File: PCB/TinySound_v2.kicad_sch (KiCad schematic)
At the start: 9 parts

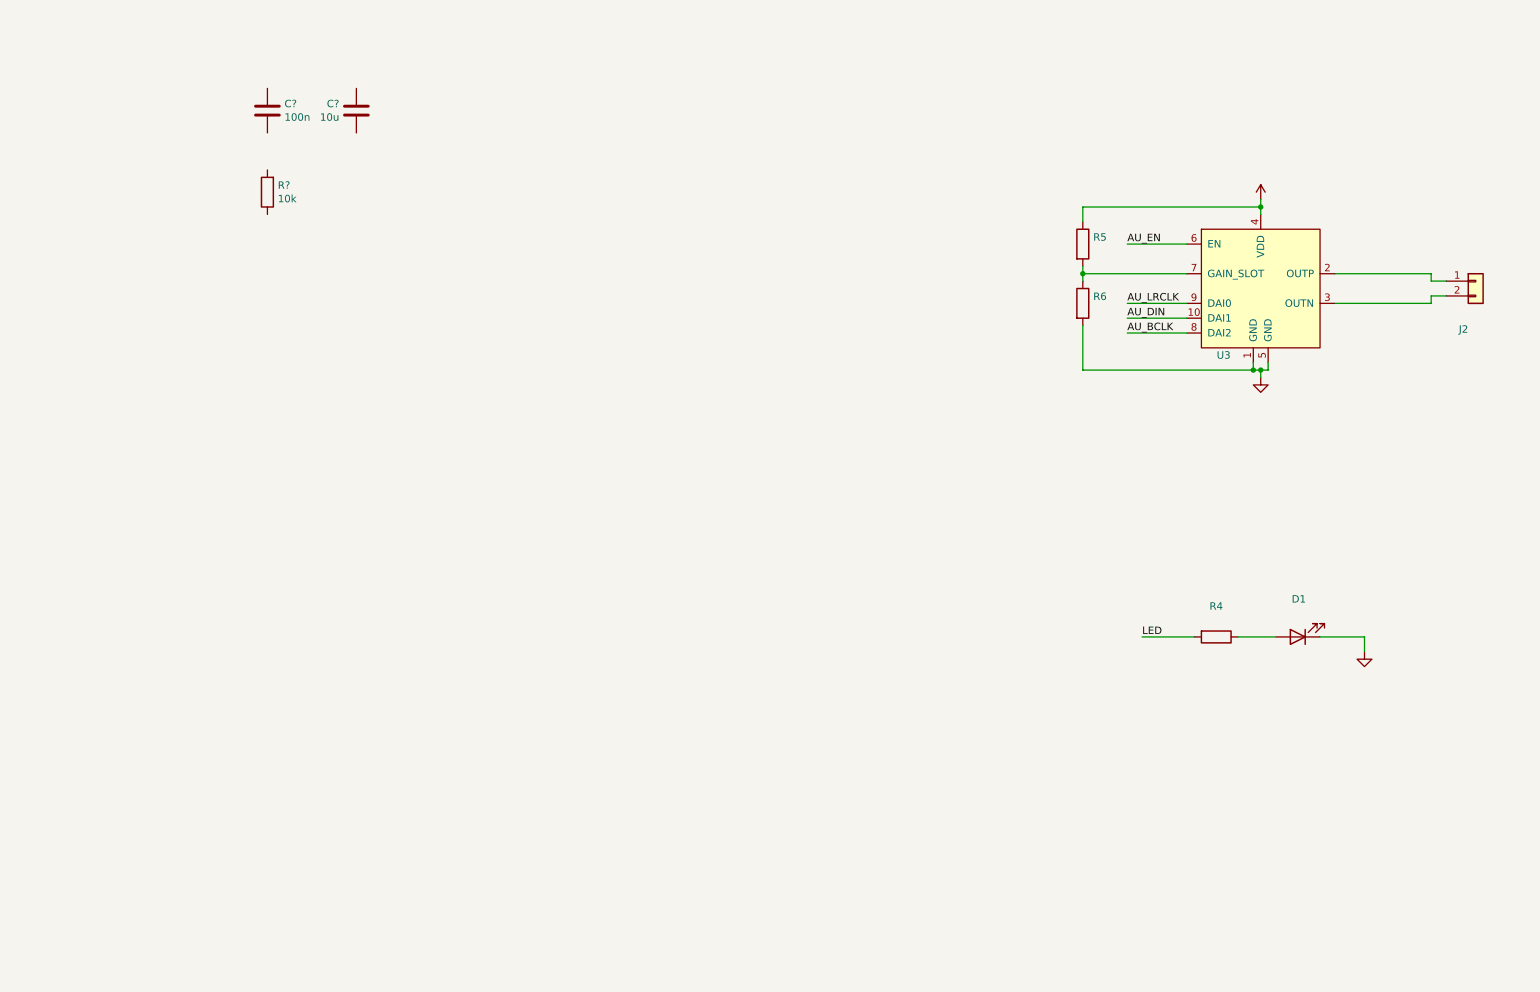
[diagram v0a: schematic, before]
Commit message: Added all components in schematic
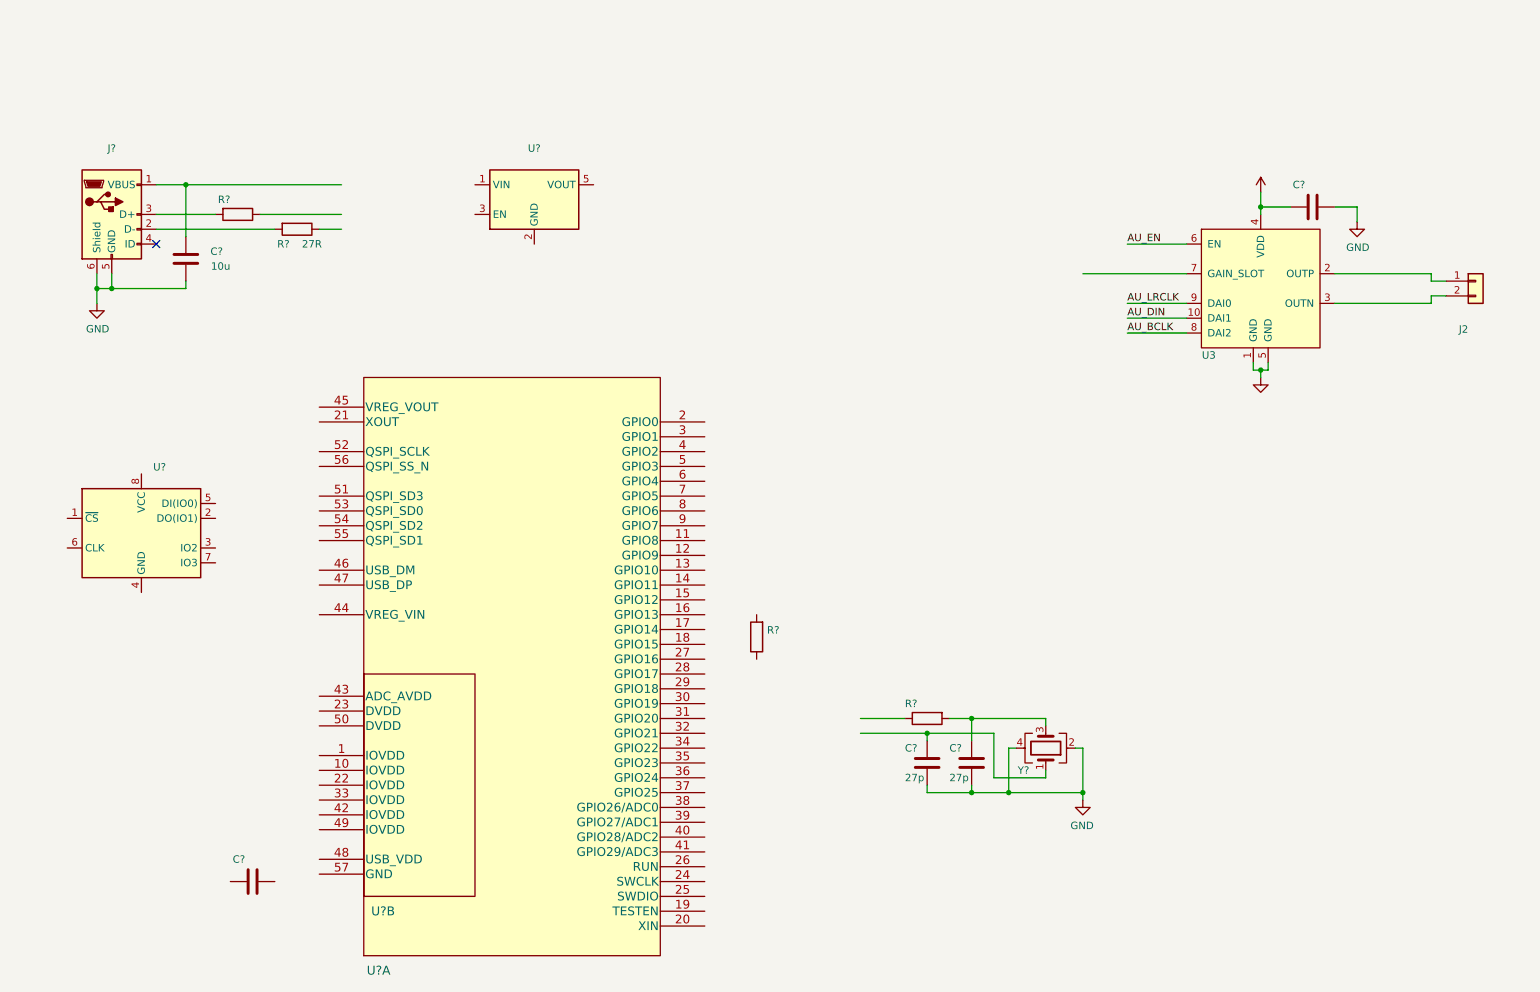
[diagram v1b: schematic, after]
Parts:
- removed D1: (no value), symbol Device:LED
- removed R4, R5, R6: (no value), symbol Device:R
- added C? (x2): 27p, Capacitor_SMD:C_0402_1005Metric, symbol Device:C
- added C?: (no value), symbol Device:C
- added J?: (no value), symbol Connector:USB_B_Micro
- added R?: (no value), symbol Device:R
- added R?: 27R, Resistor_SMD:R_0402_1005Metric, symbol Device:R
- added R?: (no value), Resistor_SMD:R_0402_1005Metric, symbol Device:R
- added U?: (no value), symbol Regulator_Linear:MIC5504-3.3YM5
- added U?: (no value), symbol Memory_Flash:W25Q128JVS
- added U? (x2): (no value), symbol TinySound:RP2040
- added Y?: (no value), symbol Device:Crystal_GND24
- C?: footprint Capacitor_SMD:C_0603_1608Metric -> (none)
- C?: value 100n -> (none); footprint Capacitor_SMD:C_0603_1608Metric -> (none)
- R?: value 10k -> (none); footprint Resistor_SMD:R_0603_1608Metric -> (none)
- U3: footprint (none) -> TinySound:FC2QFN-10
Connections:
- net +3V3: now also C?.1
- net GND: now also C?.1, C?.2, C?.1, C?.1, J?.5 (GND), J?.6 (Shield), Y?.2, Y?.4
- net at C?.2: now also J?.1 (VBUS)
- new net: J?.3 (D+), R?.2
- new net: C?.2, Y?.1
- new net: C?.2, R?.2, Y?.3
- new net: J?.2 (D-), R?.2
- no-connect marks 0 -> 1
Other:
- moved on the sheet: C?, R?

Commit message: RP2040 power, flash, crystal and reset
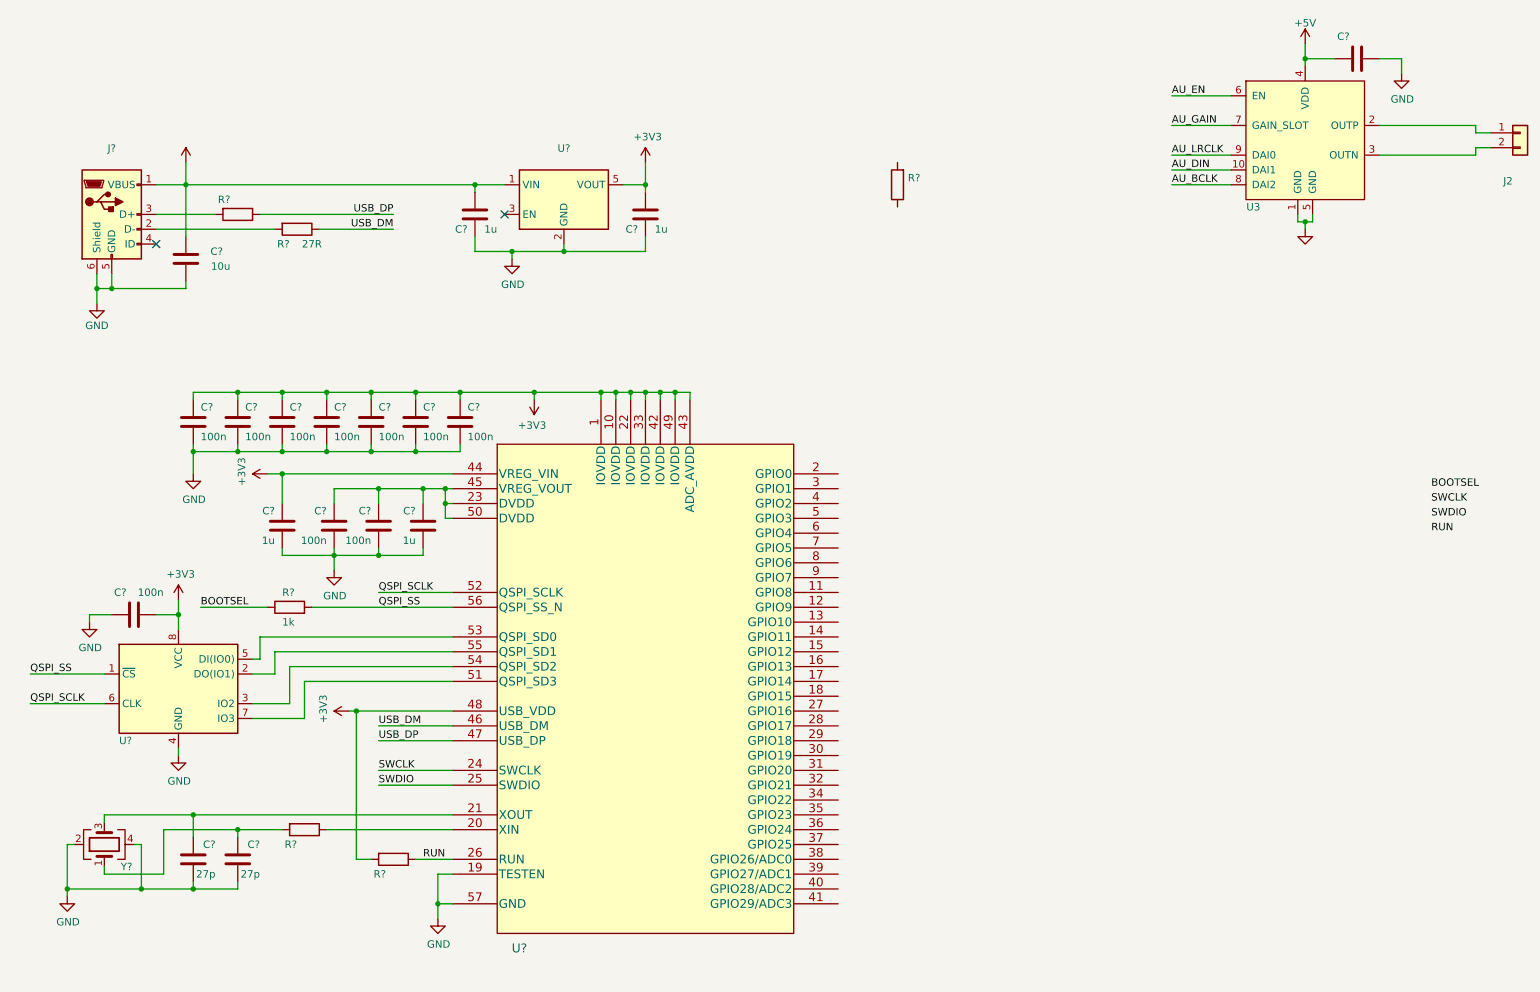
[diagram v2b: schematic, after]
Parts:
- removed C?: (no value), symbol Device:C
- removed U?: (no value), symbol TinySound:RP2040
- added C? (x10): 100n, Capacitor_SMD:C_0402_1005Metric, symbol Device:C
- added C? (x4): 1u, Capacitor_SMD:C_0402_1005Metric, symbol Device:C
- added R?: (no value), Resistor_SMD:R_0402_1005Metric, symbol Device:R
- added R?: 1k, Resistor_SMD:R_0402_1005Metric, symbol Device:R
- U?: footprint (none) -> Package_TO_SOT_SMD:SOT-23-5
- U?: footprint (none) -> Package_SO:SOIC-8_5.23x5.23mm_P1.27mm
- U?: footprint (none) -> TinySound:QFN-56_EP_7x7_Pitch0.4mm
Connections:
- net +3V3: now also U?.1 (IOVDD), U?.10 (IOVDD), U?.22 (IOVDD), U?.33 (IOVDD), U?.42 (IOVDD), U?.43 (ADC_AVDD), U?.44 (VREG_VIN), U?.48 (USB_VDD), U?.49 (IOVDD), U?.5 (VOUT), U?.8 (VCC), C?.2, C?.2, C?.2, C?.2, C?.2, C?.2, C?.2, C?.2, C?.2, C?.2, R?.2; no longer C?.1, U3.4 (VDD)
- net GND: now also U?.19 (TESTEN), U?.2 (GND), U?.4 (GND), U?.57 (GND), C?.1, C?.1, C?.1, C?.1, C?.1, C?.1, C?.1, C?.1, C?.1, C?.1, C?.1, C?.1, C?.1, C?.1
- net AU_GAIN: now reaches U3.7 (GAIN_SLOT)
- net +5V: now reaches U?.1 (VIN)
- net +5V: now also C?.1, C?.2, J?.1 (VBUS), U3.4 (VDD), C?.2
- net USB_DP: now reaches R?.1
- net USB_DP: now also U?.47 (USB_DP)
- net at C?.2, Y?.1: now also R?.2
- net at C?.2, Y?.3: now also U?.21 (XOUT); no longer R?.2
- net QSPI_SS: now reaches U?.1 (~{CS})
- net QSPI_SS: now also U?.56 (QSPI_SS_N), R?.2
- net at U?.2 (DO(IO1)): now also U?.55 (QSPI_SD1)
- net at U?.3 (IO2): now also U?.54 (QSPI_SD2)
- net at U?.5 (DI(IO0)): now also U?.53 (QSPI_SD0)
- net QSPI_SCLK: now reaches U?.6 (CLK)
- net QSPI_SCLK: now also U?.52 (QSPI_SCLK)
- net at U?.7 (IO3): now also U?.51 (QSPI_SD3)
- net USB_DM: now reaches R?.1
- net USB_DM: now also U?.46 (USB_DM)
- net at U?.20 (XIN): now also R?.1
- net SWCLK: now reaches U?.24 (SWCLK)
- net SWDIO: now reaches U?.25 (SWDIO)
- net RUN: now reaches U?.26 (RUN)
- net RUN: now also R?.1
- net at U?.45 (VREG_VOUT): now also U?.23 (DVDD), U?.50 (DVDD), C?.2, C?.2, C?.2
- new net BOOTSEL: R?.1
- no-connect marks 1 -> 2
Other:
- moved on the sheet: C?, J2, R?, U3, U?, Y?

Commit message: Finished first version of schematic
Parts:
- removed R?: (no value), symbol Device:R
- added J?: Conn_01x07, symbol Connector_Generic:Conn_01x07
- added J?: (no value), symbol Connector_Generic:Conn_01x07
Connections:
- net +3V3: now also J?.2 (Pin_2)
- net +5V: now also J?.1 (Pin_1)
- net AU_BCLK: now also U?.6 (GPIO4)
- net AU_DIN: now also U?.8 (GPIO6)
- net AU_LRCLK: now also U?.7 (GPIO5)
- net BOOTSEL: now also J?.3 (Pin_3)
- net GND: now also J?.7 (Pin_7), J?.7 (Pin_7)
- net RUN: now also J?.6 (Pin_6)
- net SWCLK: now also J?.4 (Pin_4)
- net SWDIO: now also J?.5 (Pin_5)
- net at C?.2, Y?.1: now also U?.20 (XIN); no longer R?.2
- net at C?.2, Y?.3: now also R?.2; no longer U?.21 (XOUT)
- net UART_TX: now reaches U?.2 (GPIO0)
- net UART_TX: now also J?.1 (Pin_1)
- net at R?.1: now also U?.21 (XOUT); no longer U?.20 (XIN)
- net UART_RX: now reaches U?.3 (GPIO1)
- net UART_RX: now also J?.2 (Pin_2)
- net GPIO/ADC: now reaches U?.38 (GPIO26/ADC0)
- net GPIO/ADC: now also J?.6 (Pin_6)
- new net GPIO1: J?.3 (Pin_3)
- new net GPIO2: J?.4 (Pin_4)
- new net GPIO3: J?.5 (Pin_5)
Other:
- moved on the sheet: C?, J2, R?, U3

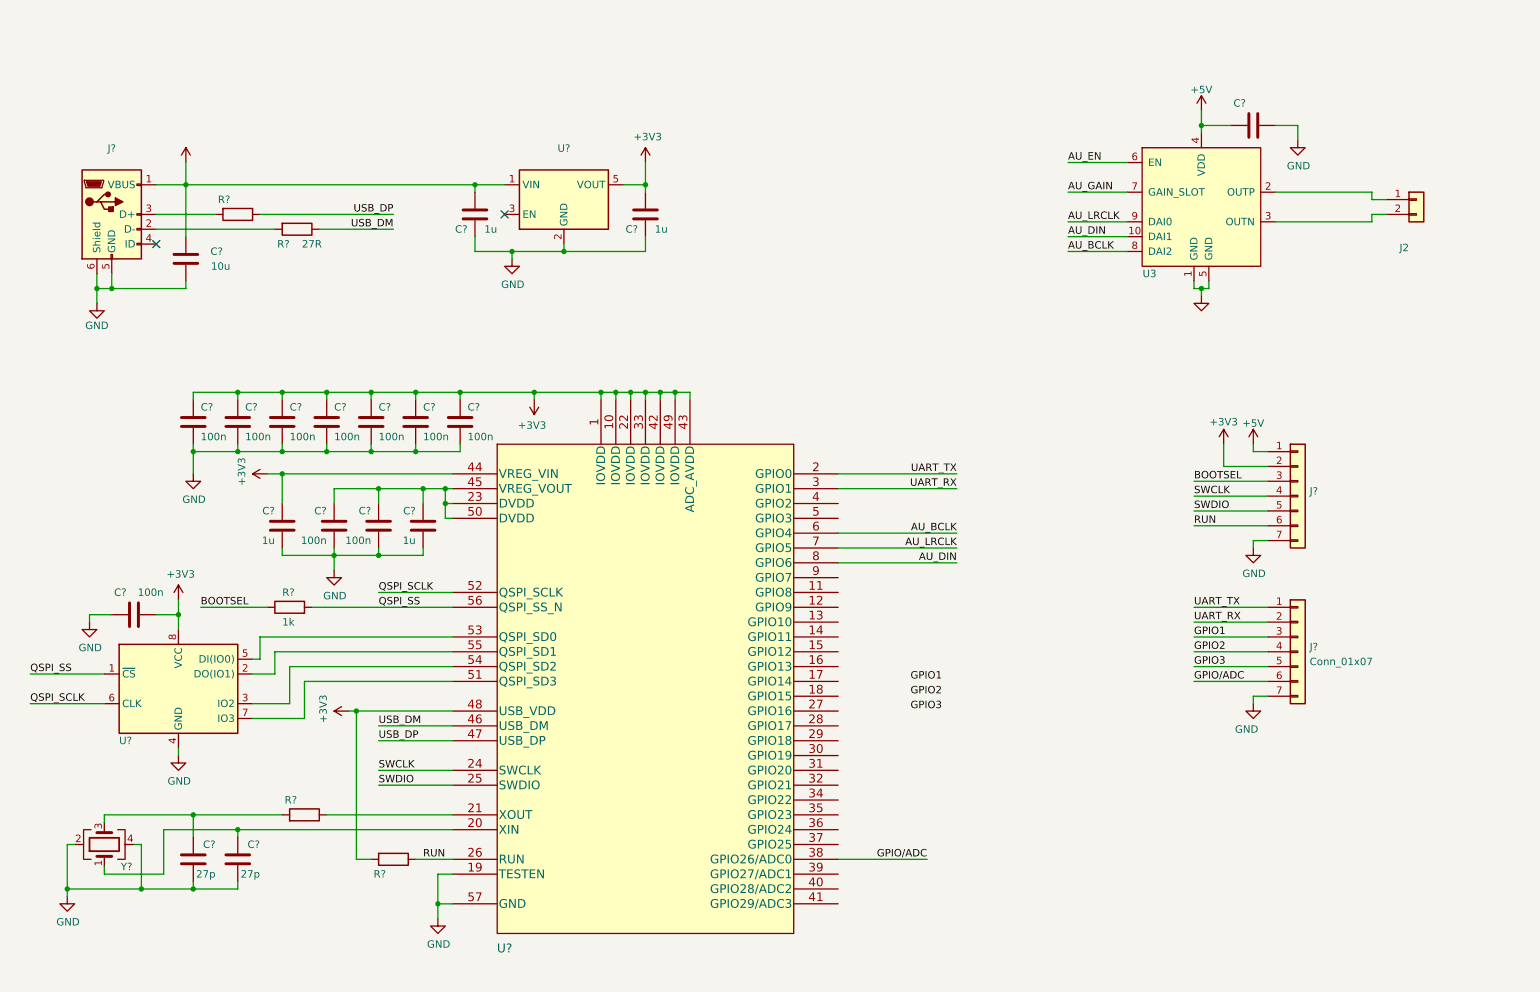
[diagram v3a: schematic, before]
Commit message: Added footprints, annoted schematic
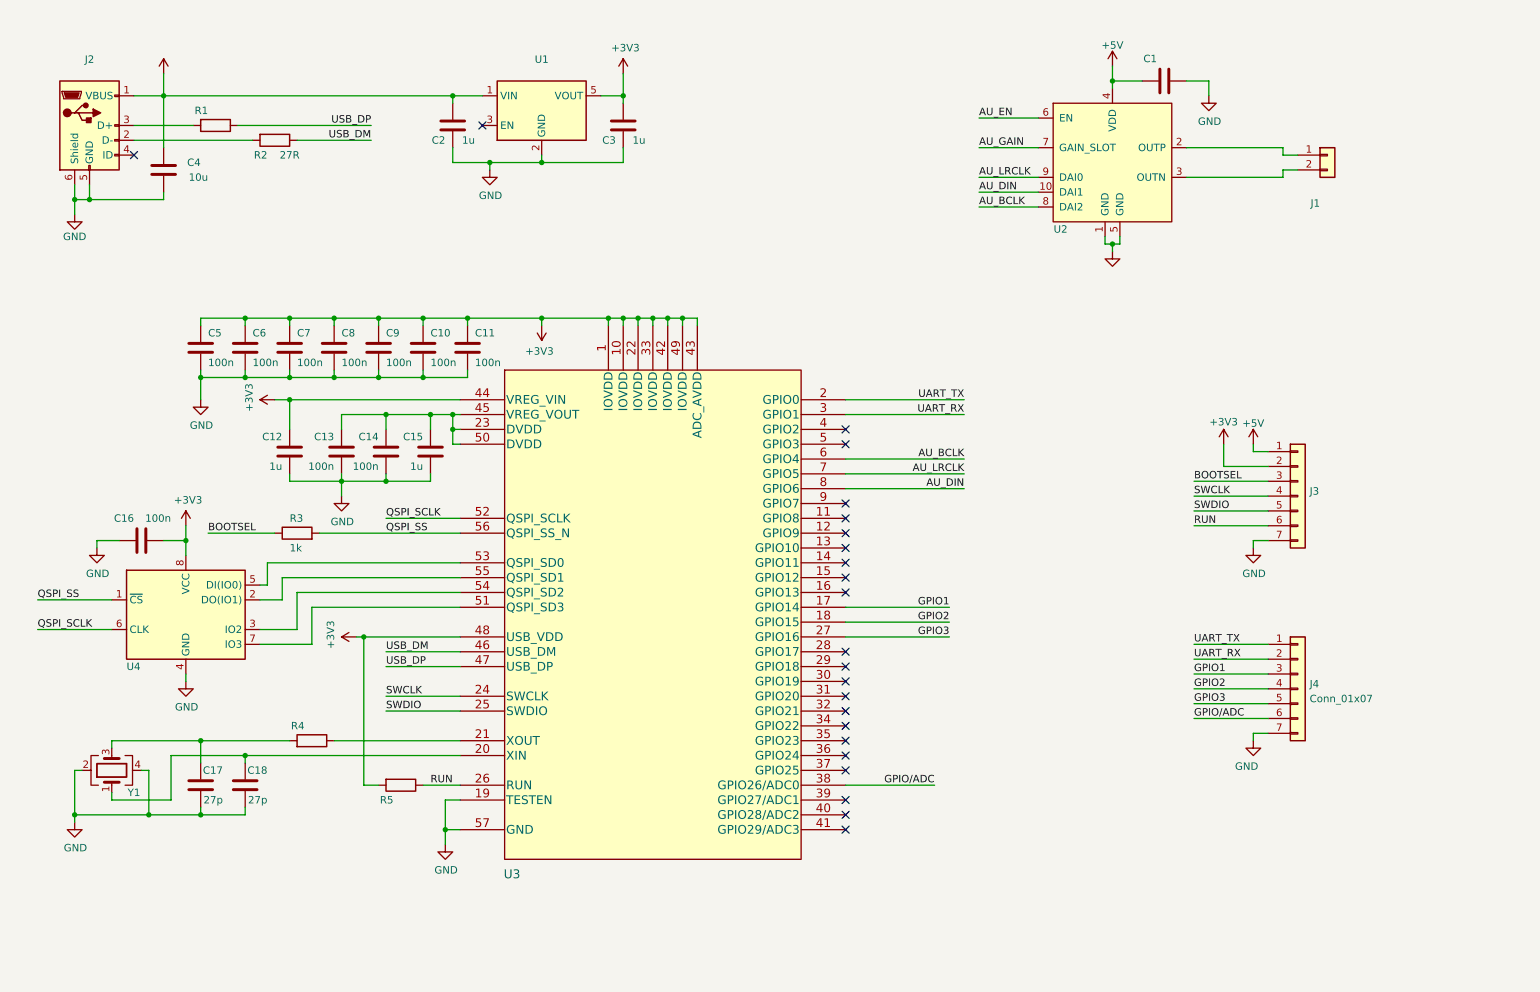
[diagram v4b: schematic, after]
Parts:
- gave numbers to parts that had none: 30
- renumbered J2 to J1, U3 to U2
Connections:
- net GPIO1: now also U3.17 (GPIO14)
- net GPIO2: now also U3.18 (GPIO15)
- net GPIO3: now also U3.27 (GPIO16)
- no-connect marks 2 -> 23
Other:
- moved on the sheet: C1, C10, C11, C12, C13, C14, C15, C16, C17, C18, C2, C3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
